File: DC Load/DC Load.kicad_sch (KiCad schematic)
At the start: 11 parts, among them J1 VSENSE, J2 LOAD_POS, J3 LOAD_NEG, U6 STM32F103C8Tx, U8 OPA2182

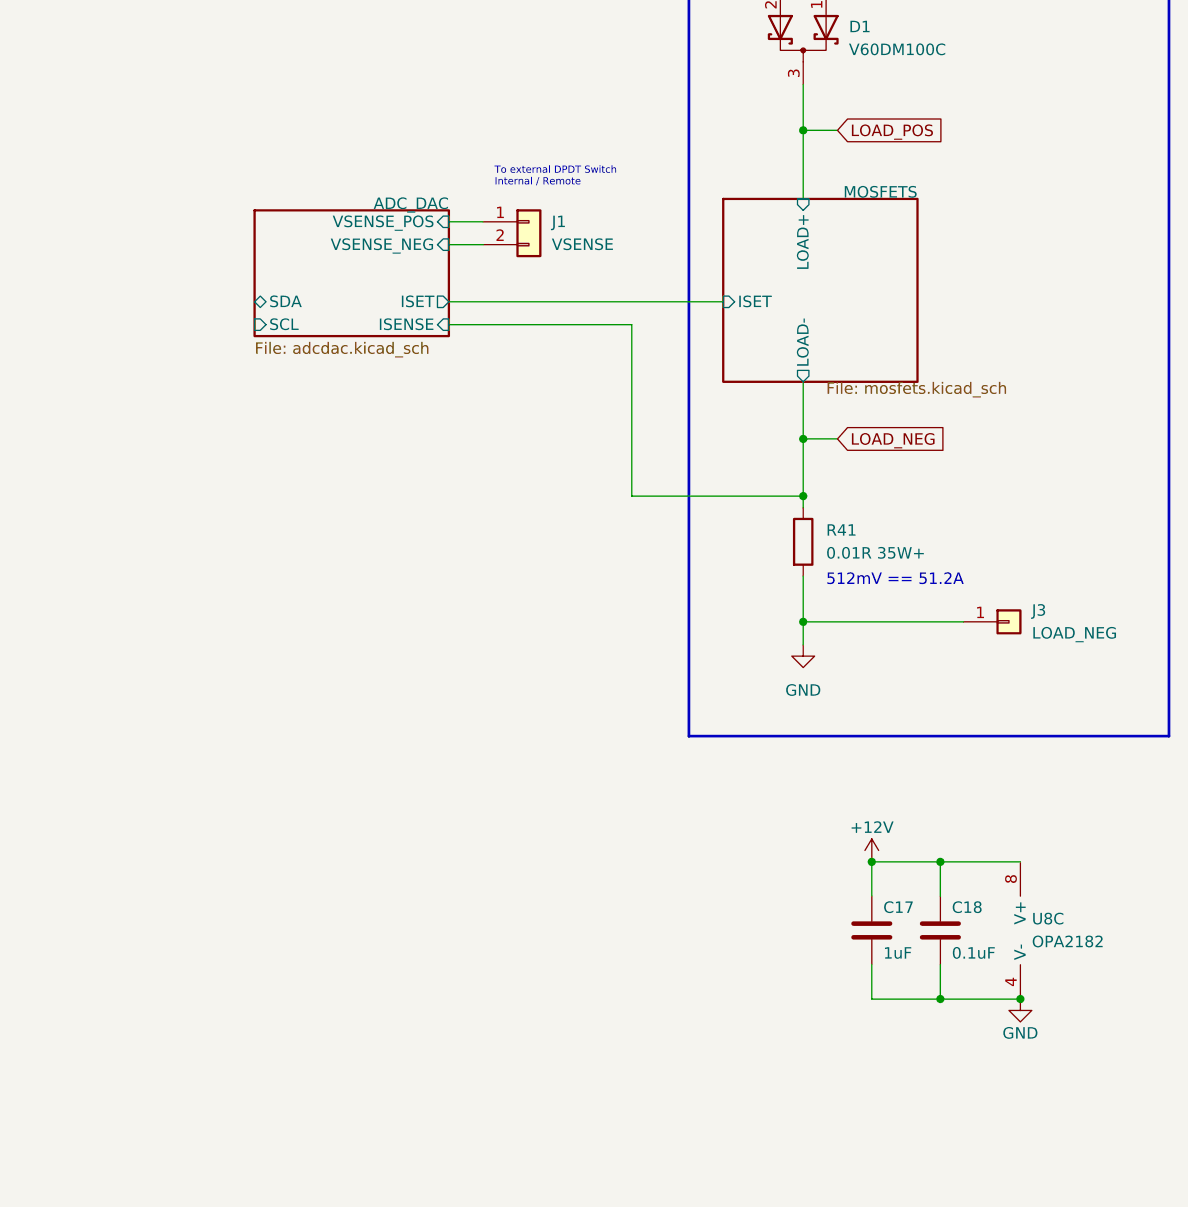
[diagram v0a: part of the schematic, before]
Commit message: Swap to ADS131 ADC
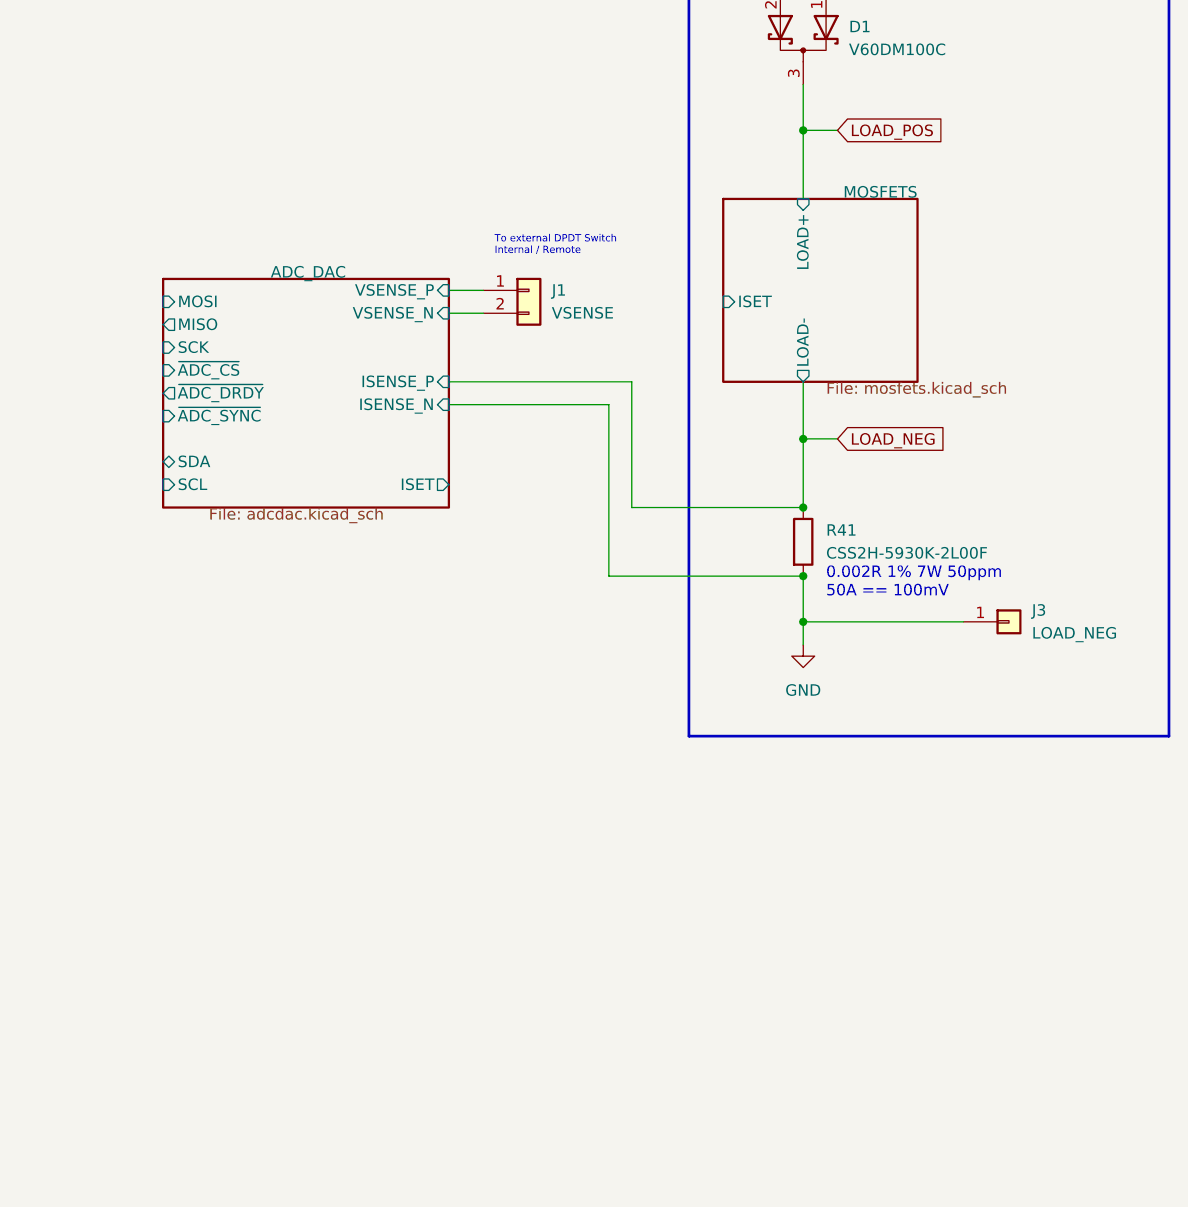
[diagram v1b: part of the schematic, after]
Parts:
- removed C17: 1uF, symbol Device:C
- removed C18: 0.1uF, symbol Device:C
- removed U8: OPA2182, symbol Device:Opamp_Dual
- R41: value 0.01R 35W+ -> CSS2H-5930K-2L00F
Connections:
- net ADC_DAC/VSENSE_NEG renamed ADC_DAC/VSENSE_N
- net ADC_DAC/VSENSE_POS renamed ADC_DAC/VSENSE_P
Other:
- sheet ADC_DAC ports: added ISENSE_N, ISENSE_P, MISO, MOSI, SCK, VSENSE_N, VSENSE_P, ~{ADC_CS}, ~{ADC_DRDY}, ~{ADC_SYNC}; removed ISENSE, VSENSE_NEG, VSENSE_POS
- note added: "0.002R 1% 7W 50ppm 50A == 100mV"
- note removed: "512mV == 51.2A"
- moved on the sheet: J1

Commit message: Assign temporary footprints
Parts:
- D1: footprint (none) -> Package_TO_SOT_SMD:TO-252-2
- F1: footprint (none) -> Fuse:Fuseholder_Littelfuse_100_series_5x30mm
- J1: footprint (none) -> Connector_PinHeader_2.54mm:PinHeader_1x02_P2.54mm_Vertical
- R41: footprint (none) -> Resistor_SMD:R_4020_10251Metric
